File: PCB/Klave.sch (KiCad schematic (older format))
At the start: 77 parts, among them J2 Display, SW0 Reset, SW1 0:0, SW10 1:3, SW11 1:4, SW12 1:5, SW13 2:0, SW14 2:1, SW15 2:2, SW16 2:3, SW17 2:4, SW18 2:5, SW19 3:0, SW2 0:1, SW20 3:1, SW21 3:2, SW22 3:3, SW23 3:4, SW24 3:5, SW26 4:1, SW27 4:2, SW28 4:3, SW29 4:4, SW3 0:2, SW30 4:5, SW31 5:0, SW35 5:4, SW36 5:5, SW4 0:3, SW5 0:4, SW6 0:5, SW7 1:0, SW8 1:1, SW9 1:2, U1 ProMicro

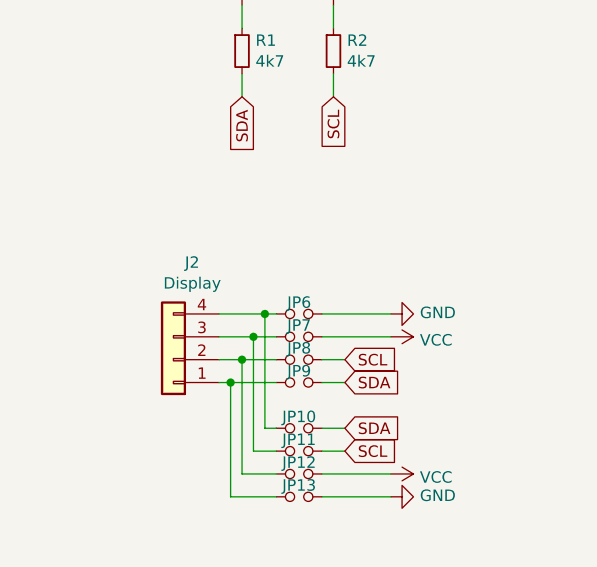
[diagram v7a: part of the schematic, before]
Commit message: Change display symbol value from "Display" to "OLED"
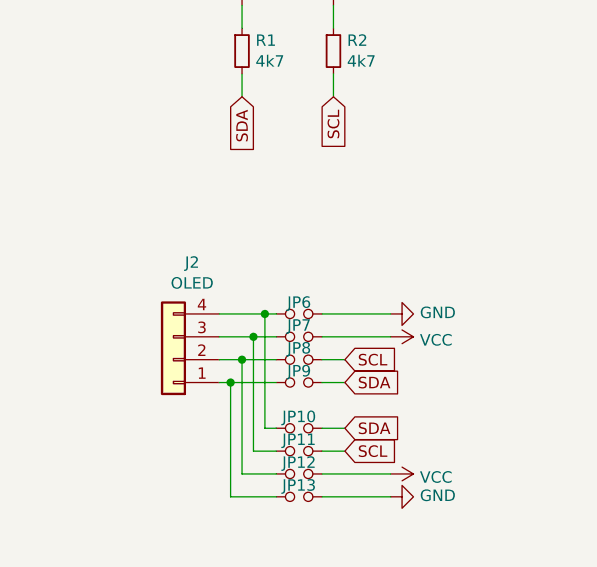
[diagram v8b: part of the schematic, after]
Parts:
- J2: value Display -> OLED
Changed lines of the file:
@@
 P 1200 6800
 F 0 "J2" H 1118 6375 50  0000 C CNN
-F 1 "Display" H 1118 6466 50  0000 C CNN
+F 1 "OLED" H 1118 6466 50  0000 C CNN
 F 2 "KlaveLib:Display_OLED_128x32" H 1200 6800 50  0001 C CNN
 F 3 "~" H 1200 6800 50  0001 C CNN
